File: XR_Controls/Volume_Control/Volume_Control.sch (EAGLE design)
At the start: 4 parts

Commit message: Licenses
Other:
- note added: "XR Passive Volume Control Project by Cycfi Research is licensed under a Creative Commons Attribution-ShareAlike 4.0 International License. Copyright CYCFI Research Inc. 2013-2016"
- note removed: "XR Controls Project by Cycfi Research is licensed under a Creative Commons Attribution-NonCommercial 4.0 International License. http://creativecommons.org/licenses/by-nc/4.0/ Copyright CYCFI Research Inc. 2013-2016"
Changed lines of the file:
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@@
 <text x="177.8" y="19.05" size="2.54" layer="95">Volume Control</text>
 <text x="253.365" y="6.985" size="2.1844" layer="95">v1.47</text>
-<text x="7.62" y="12.7" size="2.54" layer="95">XR Controls Project by Cycfi Research is licensed under a
-Creative Commons Attribution-NonCommercial 4.0 International License.
-http://creativecommons.org/licenses/by-nc/4.0/
+<text x="7.62" y="12.7" size="2.54" layer="95">XR Passive Volume Control Project by Cycfi Research is licensed under a
+Creative Commons Attribution-ShareAlike 4.0 International License.
 Copyright CYCFI Research Inc. 2013-2016</text>
 <text x="200.66" y="11.43" size="2.54" layer="95">2016040</text>

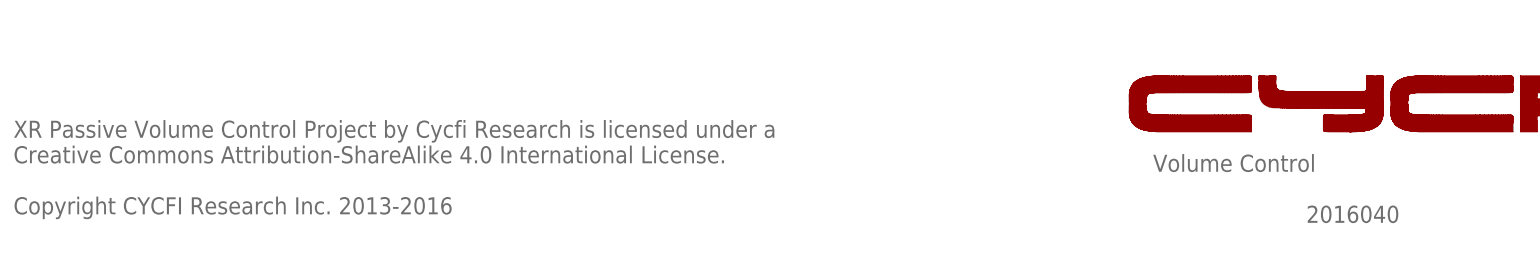
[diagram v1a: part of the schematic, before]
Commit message: *organize 5-waay switch and its configuration board(a and b) *update license date *remove red frame schem pdf files, change with black frame *update document number
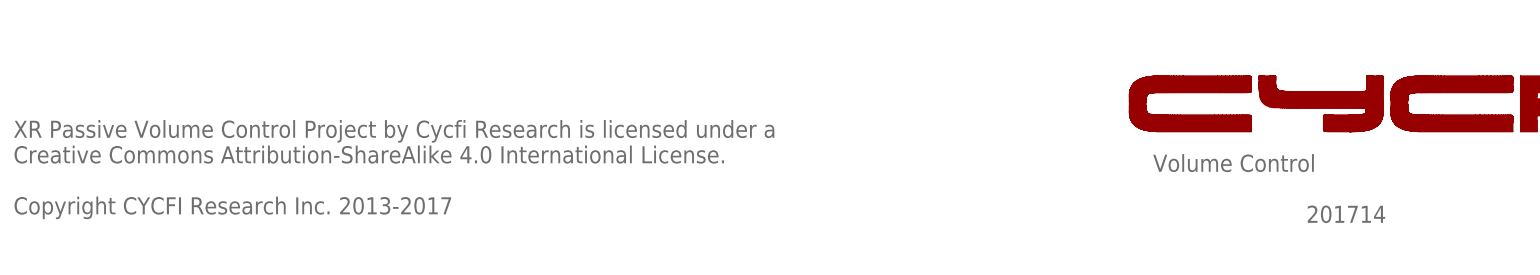
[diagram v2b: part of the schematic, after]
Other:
- note added: "201714"
- note added: "XR Passive Volume Control Project by Cycfi Research is licensed under a Creative Commons Attribution-ShareAlike 4.0 International License. Copyright CYCFI Research Inc. 2013-2017"
- note removed: "2016040"
- note removed: "XR Passive Volume Control Project by Cycfi Research is licensed under a Creative Commons Attribution-ShareAlike 4.0 International License. Copyright CYCFI Research Inc. 2013-2016"
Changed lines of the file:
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@@
 <text x="7.62" y="12.7" size="2.54" layer="95">XR Passive Volume Control Project by Cycfi Research is licensed under a
 Creative Commons Attribution-ShareAlike 4.0 International License.
-Copyright CYCFI Research Inc. 2013-2016</text>
-<text x="200.66" y="11.43" size="2.54" layer="95">2016040</text>
+Copyright CYCFI Research Inc. 2013-2017</text>
+<text x="200.66" y="11.43" size="2.54" layer="95">201714</text>
 <wire x1="192.47528125" y1="25.047221875" x2="190.115640625" y2="25.047221875" width="0" layer="94"/>
 <wire x1="190.115640625" y1="25.047221875" x2="188.10833125" y2="25.047225" width="0" layer="94"/>

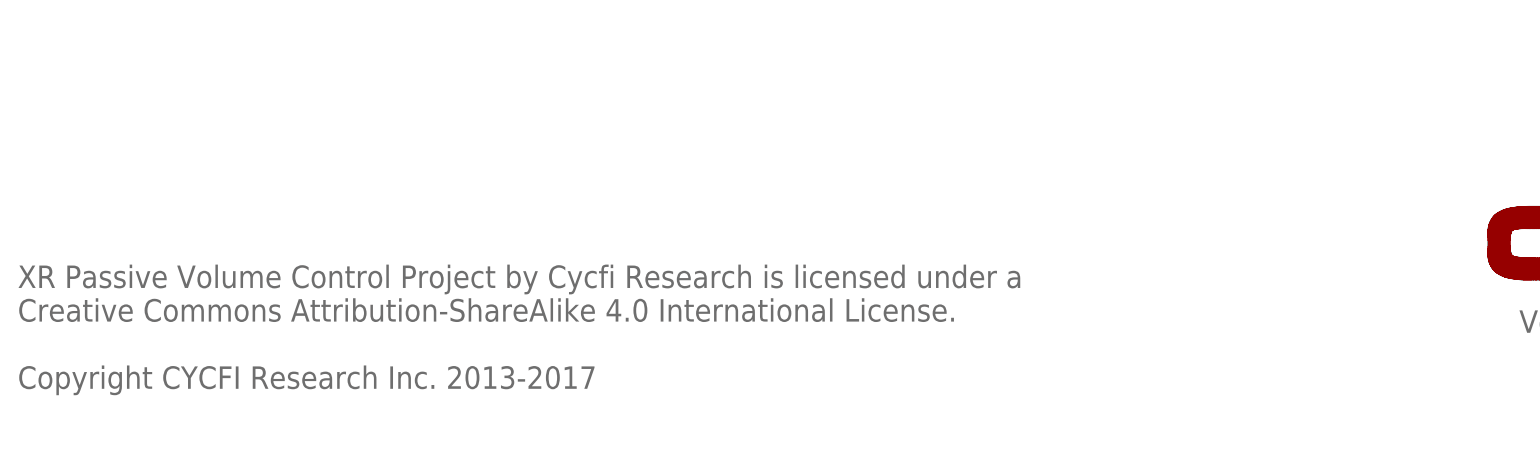
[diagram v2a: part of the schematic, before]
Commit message: Updated broken .sch files
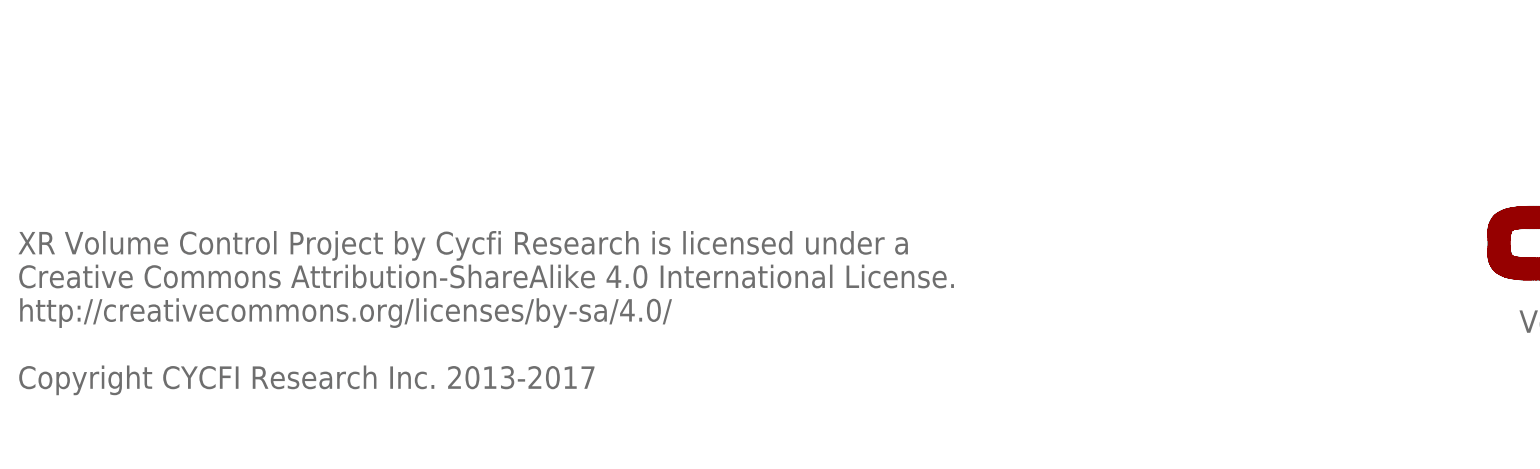
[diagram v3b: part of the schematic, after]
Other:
- note added: "XR Volume Control Project by Cycfi Research is licensed under a Creative Commons Attribution-ShareAlike 4.0 International License. http://creativecommons.org/licenses/by-sa/4.0/ Copyright CYCFI Research Inc. 2013-2017"
- note removed: "XR Passive Volume Control Project by Cycfi Research is licensed under a Creative Commons Attribution-ShareAlike 4.0 International License. Copyright CYCFI Research Inc. 2013-2017"
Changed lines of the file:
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@@
 <text x="110.49" y="107.95" size="1.778" layer="95">POT1
 25K</text>
-<text x="177.8" y="19.05" size="2.54" layer="95">Volume Control</text>
-<text x="253.365" y="6.985" size="2.1844" layer="95">v1.47</text>
-<text x="7.62" y="12.7" size="2.54" layer="95">XR Passive Volume Control Project by Cycfi Research is licensed under a
+<text x="177.8" y="19.05" size="2.54" layer="95" font="vector">Volume Control</text>
+<text x="253.365" y="6.985" size="2.1844" layer="95" font="vector">v1.47</text>
+<text x="7.62" y="12.7" size="2.54" layer="95" font="vector">XR Volume Control Project by Cycfi Research is licensed under a
 Creative Commons Attribution-ShareAlike 4.0 International License.
+http://creativecommons.org/licenses/by-sa/4.0/
 Copyright CYCFI Research Inc. 2013-2017</text>
-<text x="200.66" y="11.43" size="2.54" layer="95">201714</text>
+<text x="200.66" y="11.43" size="2.54" layer="95" font="vector">201714</text>
 <wire x1="192.47528125" y1="25.047221875" x2="190.115640625" y2="25.047221875" width="0" layer="94"/>
 <wire x1="190.115640625" y1="25.047221875" x2="188.10833125" y2="25.047225" width="0" layer="94"/>
